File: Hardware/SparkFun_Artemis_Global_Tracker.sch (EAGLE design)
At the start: 148 parts, among them J1 IRIDIUM_9603N, J2 USB-C, J6 U.FL, J7 ANTENNA-GROUNDEDEDGE_SMA, J8 STAND-OFF-REFLOW-M2.0_6.0MM_T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, J9 STAND-OFF-REFLOW-M2.0_6.0MM_T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, Q1 5.8A/30V/35mΩ, Q2 20V/4.2A/52mΩ/1.4W, Q3 20V/4.2A/52mΩ/1.4W, Q4 600mA/40V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

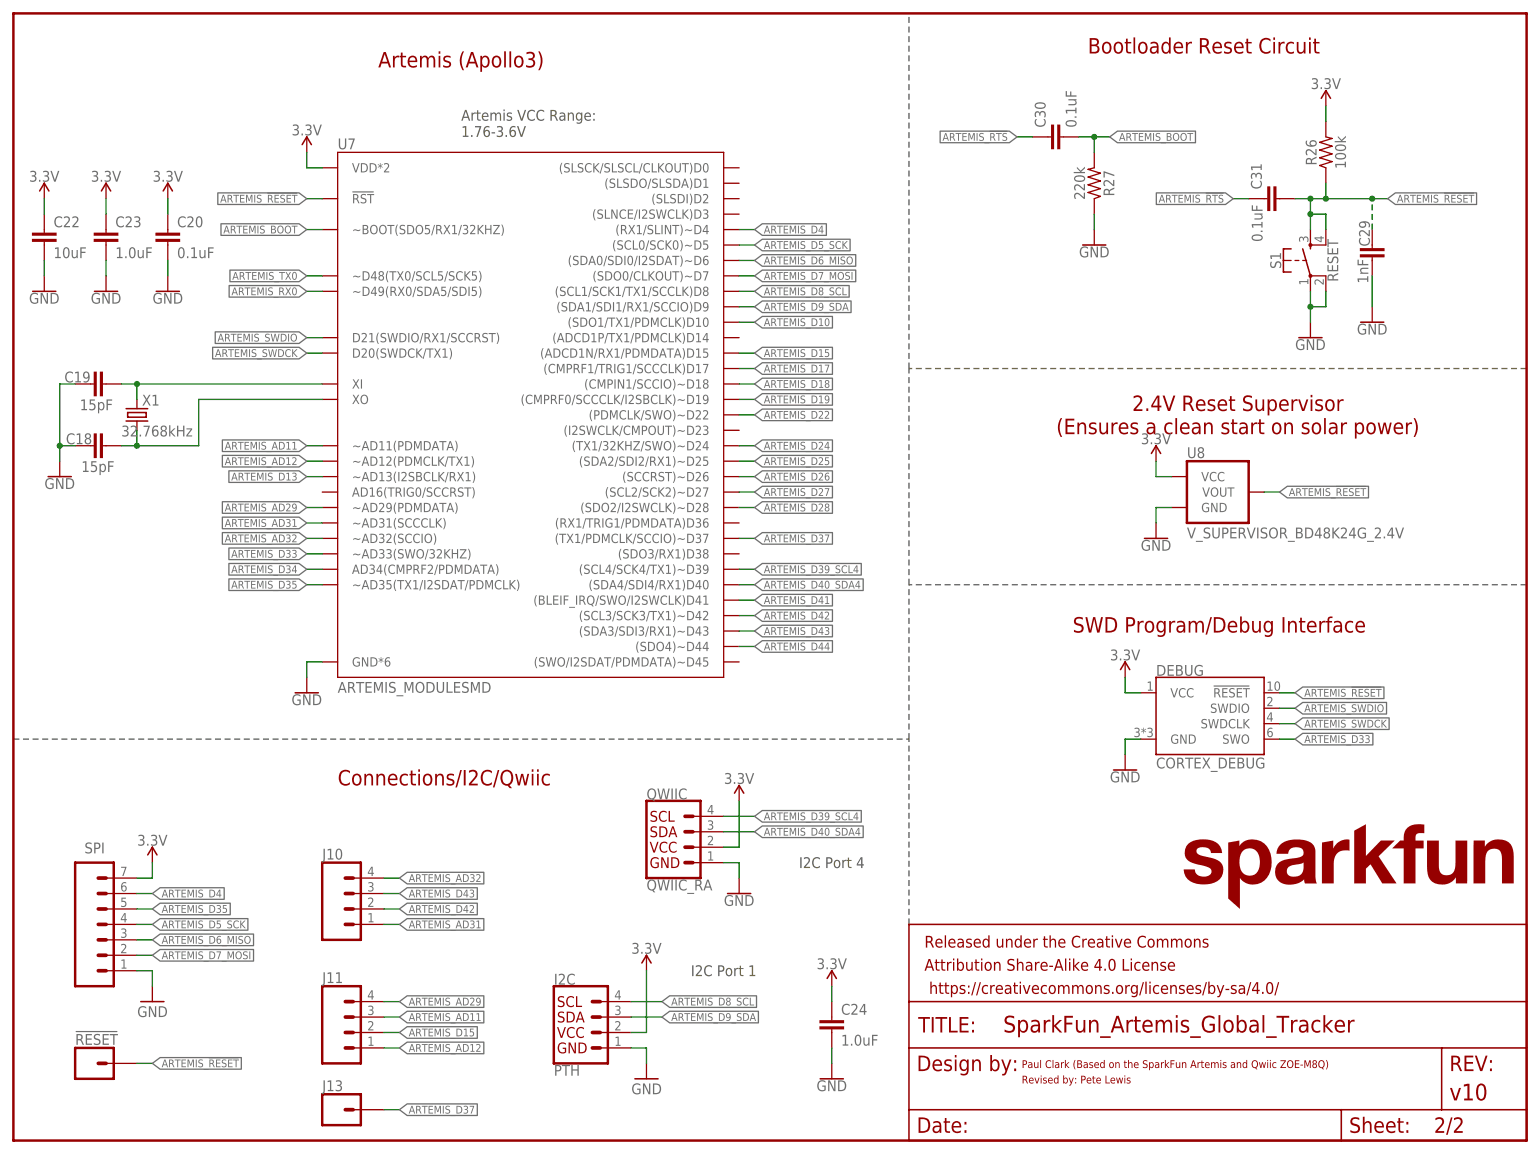
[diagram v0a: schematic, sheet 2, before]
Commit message: design review changes
-measures cleaned up to avoid overlap
-LED labels to text only (and corrected 9603N typo)
-3.3V voltage regulator text in schematic (section label)
-corrected SPI SCK label on bottom
-D35 buzzard label turned to AD35 and round end
-D4 to round end label
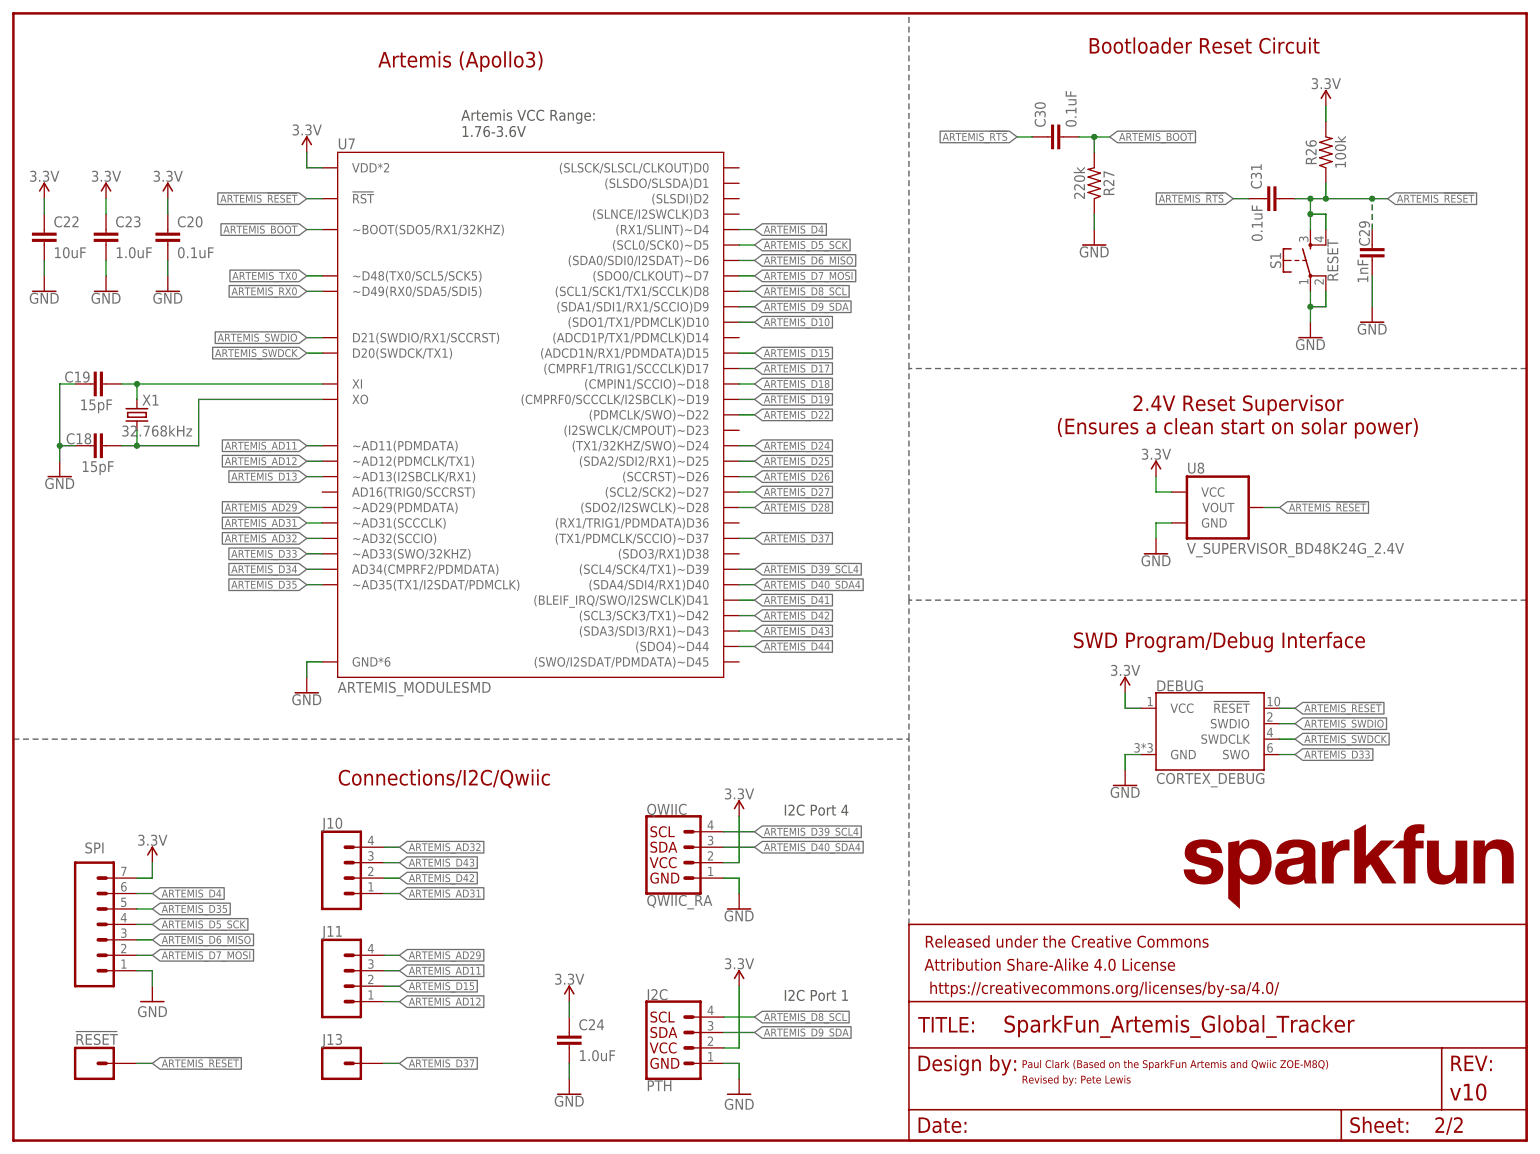
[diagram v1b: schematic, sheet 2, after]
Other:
- note added: "3.3V Voltage Regulator"
- moved on the sheet: C24, DEBUG, I2C, J10, J11, J13, QWIIC, U8

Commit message: eng checklist run
nudged some vias to avoid hitting silk labels
-fixed some PROD_IDs
-a little SCH cleaning
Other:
- moved on the sheet: 3V3EN, C1, C12, C14, C15, C16, C21, C25, C27, C28, C7, D10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

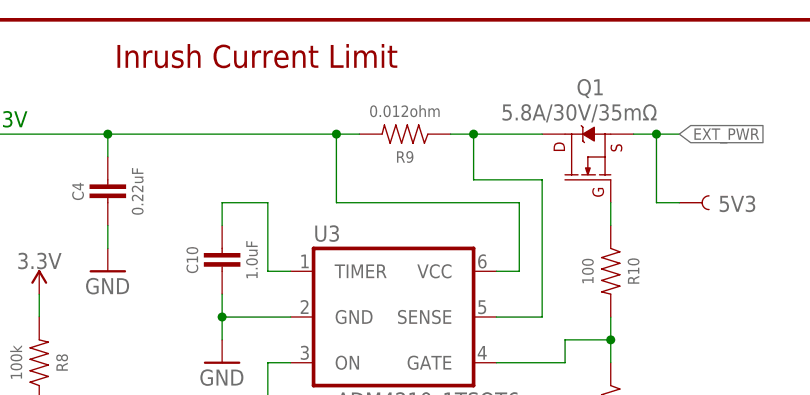
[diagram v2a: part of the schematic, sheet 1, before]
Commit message: R9 Current Sense Resistor Value changed to 15mOhm
Switched in-rush current sense resistor from 12mOhms to 15mOhms. This value is easier to source. It changes the in-rush current sense from 4.2A to 3.3A.

Also added datasheet for in-rush current protection IC: ADM4210
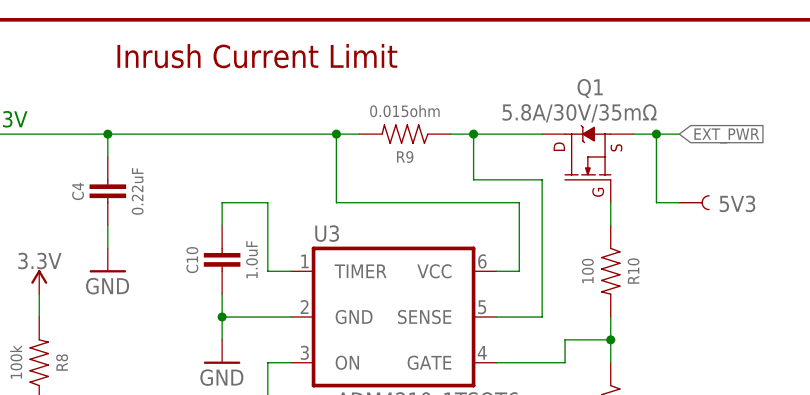
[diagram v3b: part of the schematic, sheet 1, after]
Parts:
- R9: value 0.012ohm -> 0.015ohm; device SparkFun-Resistors:0.012OHM0603 -> SparkFun-Resistors:0.015OHM_1%_1/3W_0603
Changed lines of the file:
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@@
 <part name="JP1" library="SparkFun-Jumpers" deviceset="JUMPER-SMT_3_1-NC_TRACE" device="_SILK" package3d_urn="urn:adsk.eagle:package:39288/1" value="JUMPER-SMT_3_1-NC_TRACE_SILK"/>
 <part name="R10" library="SparkFun-Resistors" deviceset="100OHM" device="-0402-TIGHT-1/16W-1%" value="100"/>
-<part name="R9" library="SparkFun-Resistors" deviceset="0.012OHM" device="0603" value="0.012ohm"/>
+<part name="R9" library="SparkFun-Resistors" deviceset="0.015OHM" device="_1%_1/3W_0603" value="0.015ohm"/>
 <part name="R11" library="SparkFun-Resistors" deviceset="100OHM" device="-0402-TIGHT-1/16W-1%" value="100"/>
 <part name="SC1+" library="SparkFun-Connectors" deviceset="CONN_01" device="PTH_NO_SILK_YES_STOP"/>

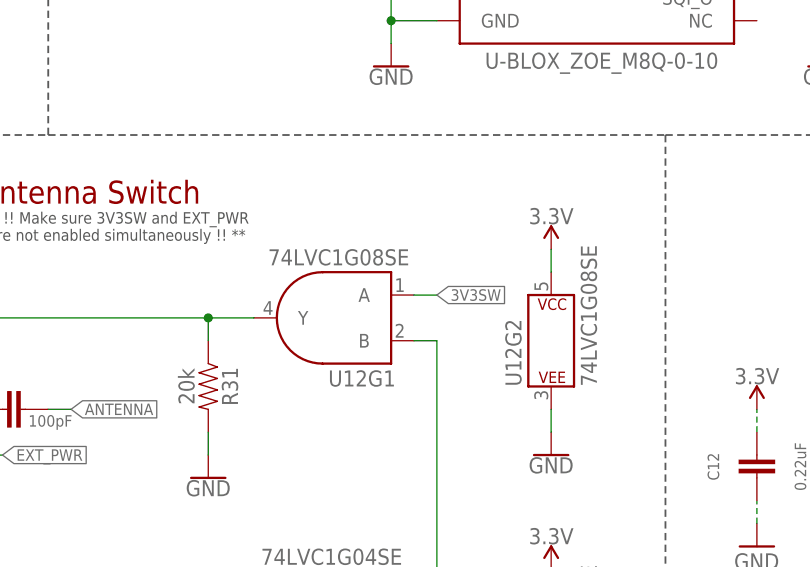
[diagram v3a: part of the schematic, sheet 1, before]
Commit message: AND Gate (U12) PROD_ID update to correct package
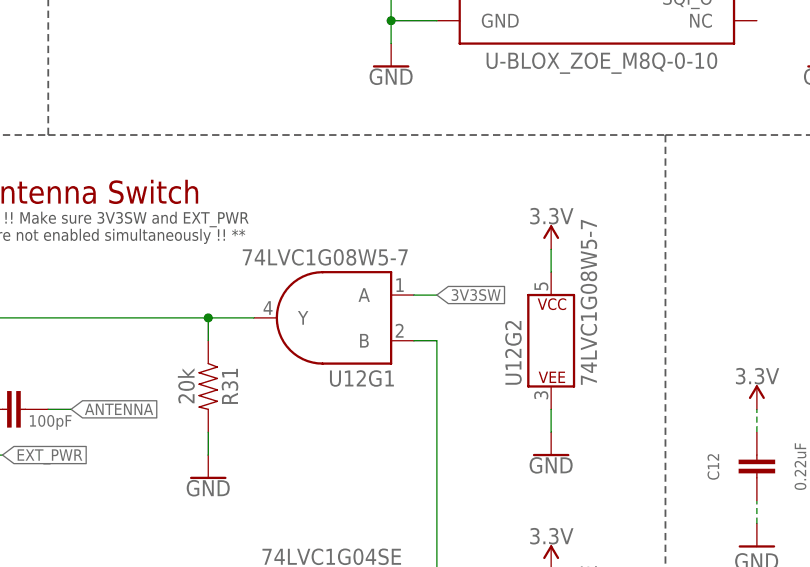
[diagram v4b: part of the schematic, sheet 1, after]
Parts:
- U12: value 74LVC1G08SE -> 74LVC1G08W5-7; device SparkFun-IC-Logic:74LVC08SE -> SparkFun-IC-Logic:74LVC08_W5-7
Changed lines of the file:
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@@
 <part name="GND44" library="SparkFun-PowerSymbols" deviceset="GND" device=""/>
 <part name="SUPPLY18" library="SparkFun-PowerSymbols" deviceset="3.3V" device=""/>
-<part name="U12" library="SparkFun-IC-Logic" deviceset="74*08" device="SE" technology="LVC" value="74LVC1G08SE"/>
+<part name="U12" library="SparkFun-IC-Logic" deviceset="74*08" device="_W5-7" technology="LVC" value="74LVC1G08W5-7"/>
 <part name="U11" library="SparkFun-IC-Logic" deviceset="74*1G04" device="SE" technology="LVC" value="74LVC1G04SE"/>
 <part name="R31" library="SparkFun-Resistors" deviceset="20KOHM" device="-0402T-1/16W-1%" value="20k"/>
